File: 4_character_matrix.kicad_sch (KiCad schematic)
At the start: 24 parts, among them U22 SN74LVC244A, U23 SM411006N/15, U24 SM411006N/15, U25 SN74LVC244A, U26 SM411006N/15, U27 SM411006N/15

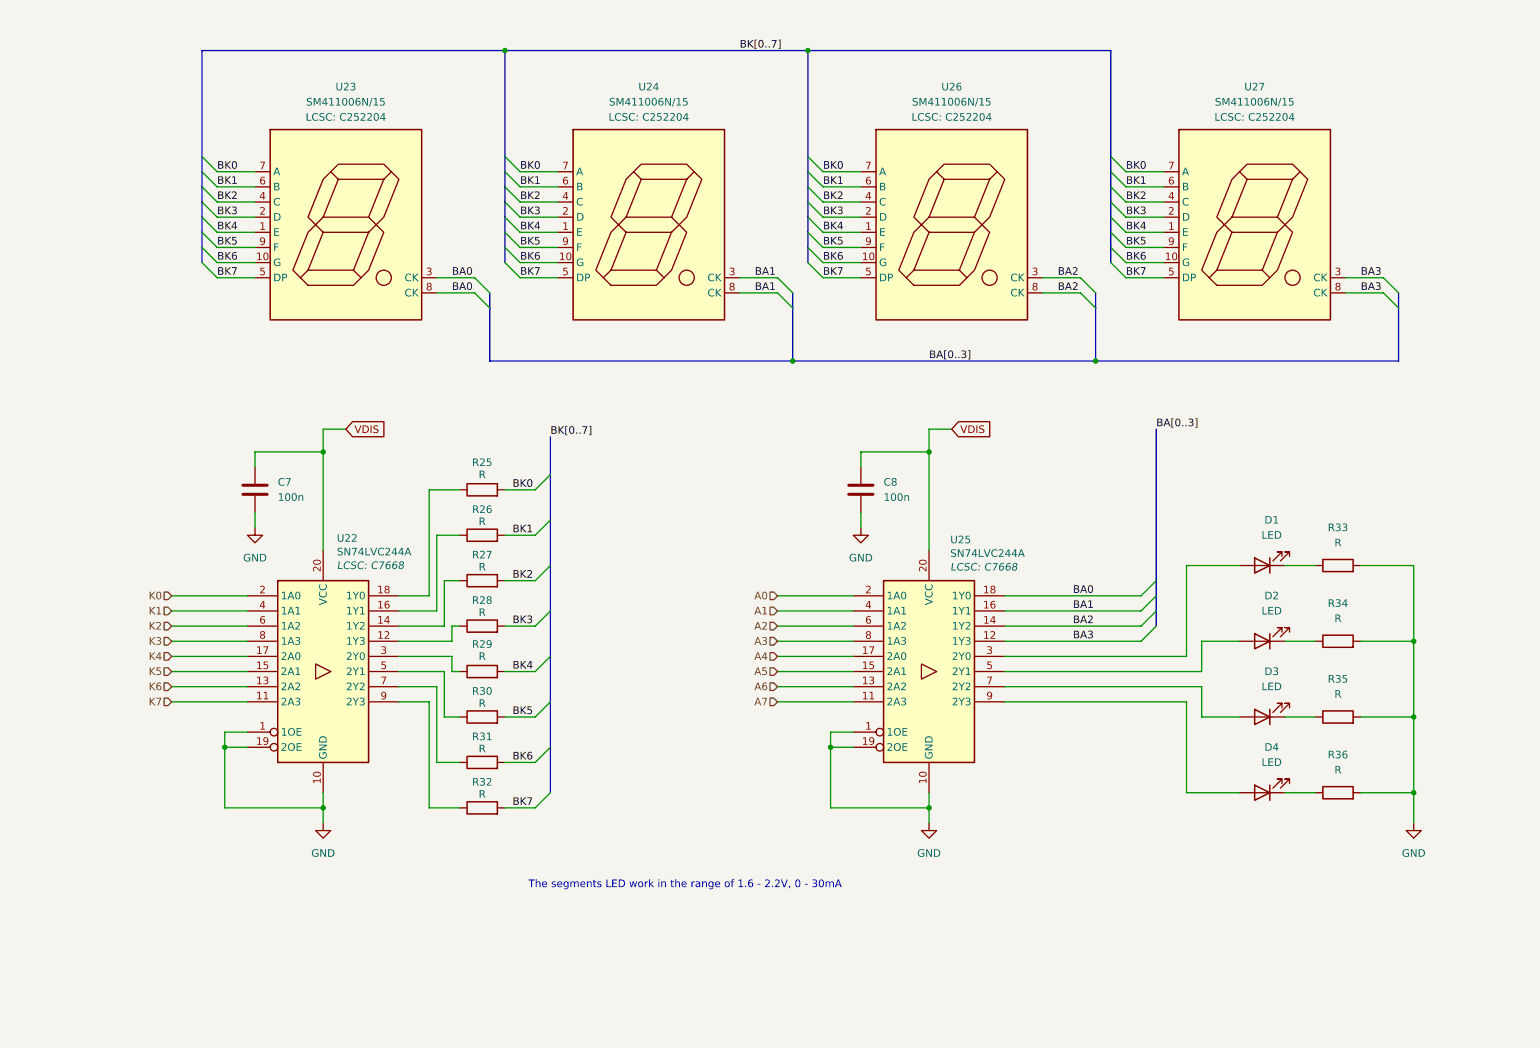
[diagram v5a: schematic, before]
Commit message: current limit resistors
- styling changes in the schematics
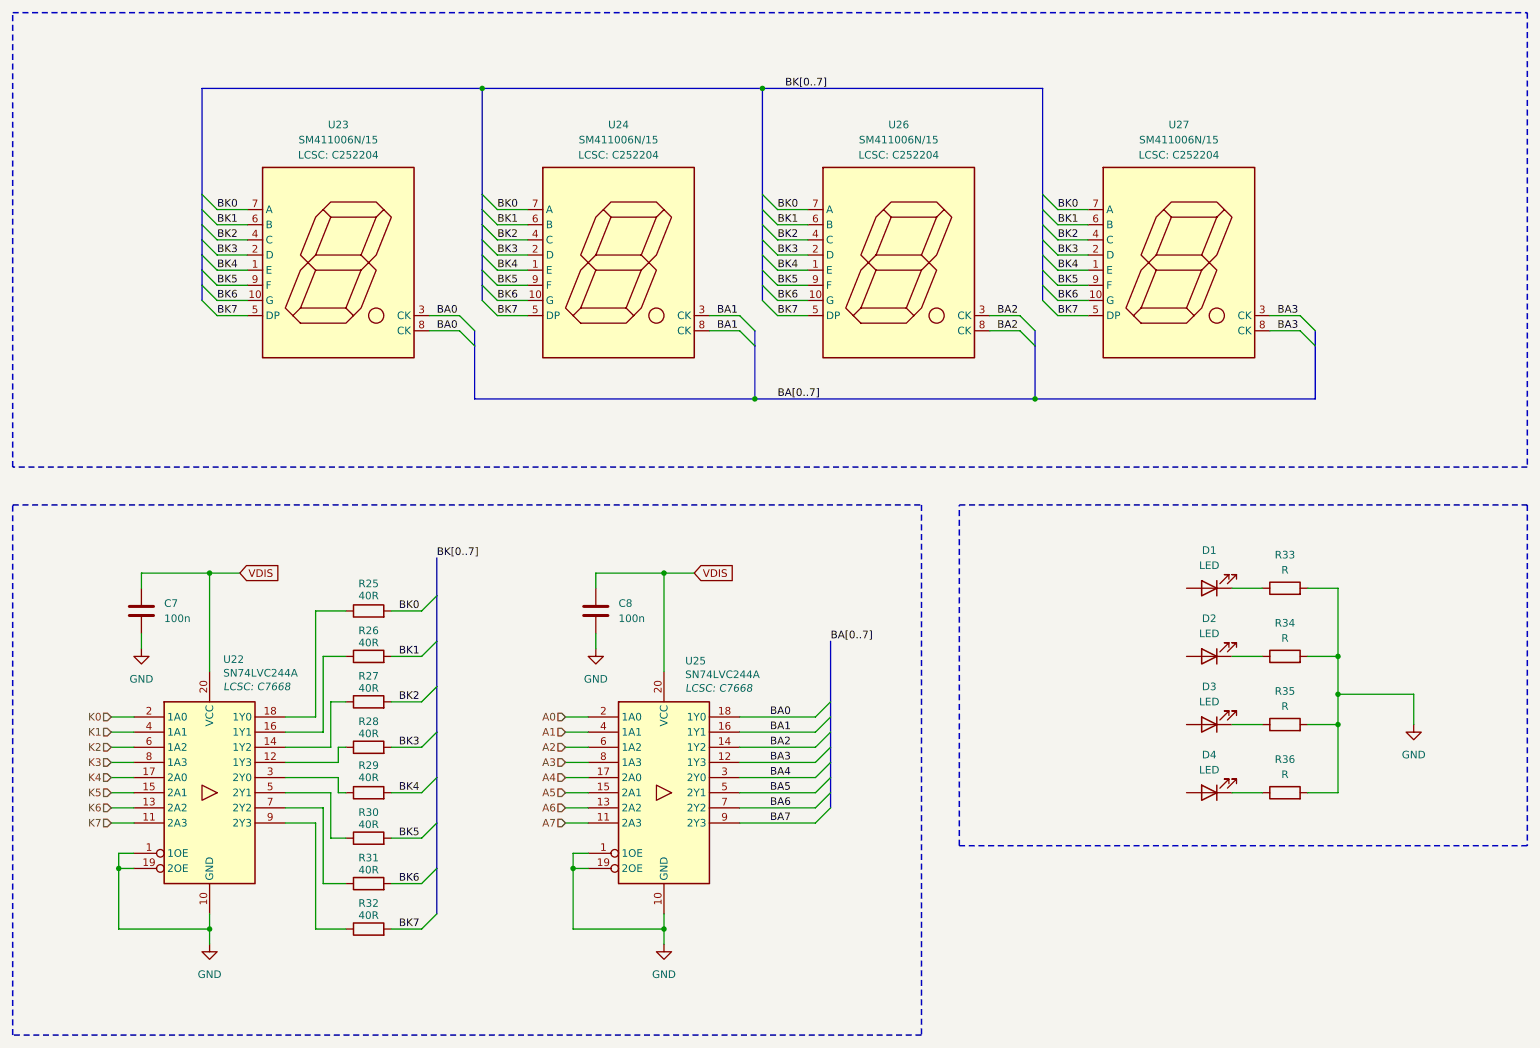
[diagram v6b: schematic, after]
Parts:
- R25, R26, R27, R28, R29, R30, R31, R32: value R -> 40R
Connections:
- net at D2.2 (A): no longer U25.5 (2Y1)
- net at D1.2 (A): no longer U25.3 (2Y0)
- net at D3.2 (A): no longer U25.7 (2Y2)
- net at D4.2 (A): no longer U25.9 (2Y3)
- new net BA4: U25.3 (2Y0)
- new net BA5: U25.5 (2Y1)
- new net BA6: U25.7 (2Y2)
- new net BA7: U25.9 (2Y3)
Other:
- note removed: "The segments LED work in the range of 1.6 - 2.2V, 0 - 30mA"
- moved on the sheet: C7, C8, D1, D2, D3, D4, R25, R26, R27, R28, R29, R30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

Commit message: minor changes
- removal of colon LEDs
- removal of test points addition of solders bridges
- time pulse LED added
- modification in MCU pinout
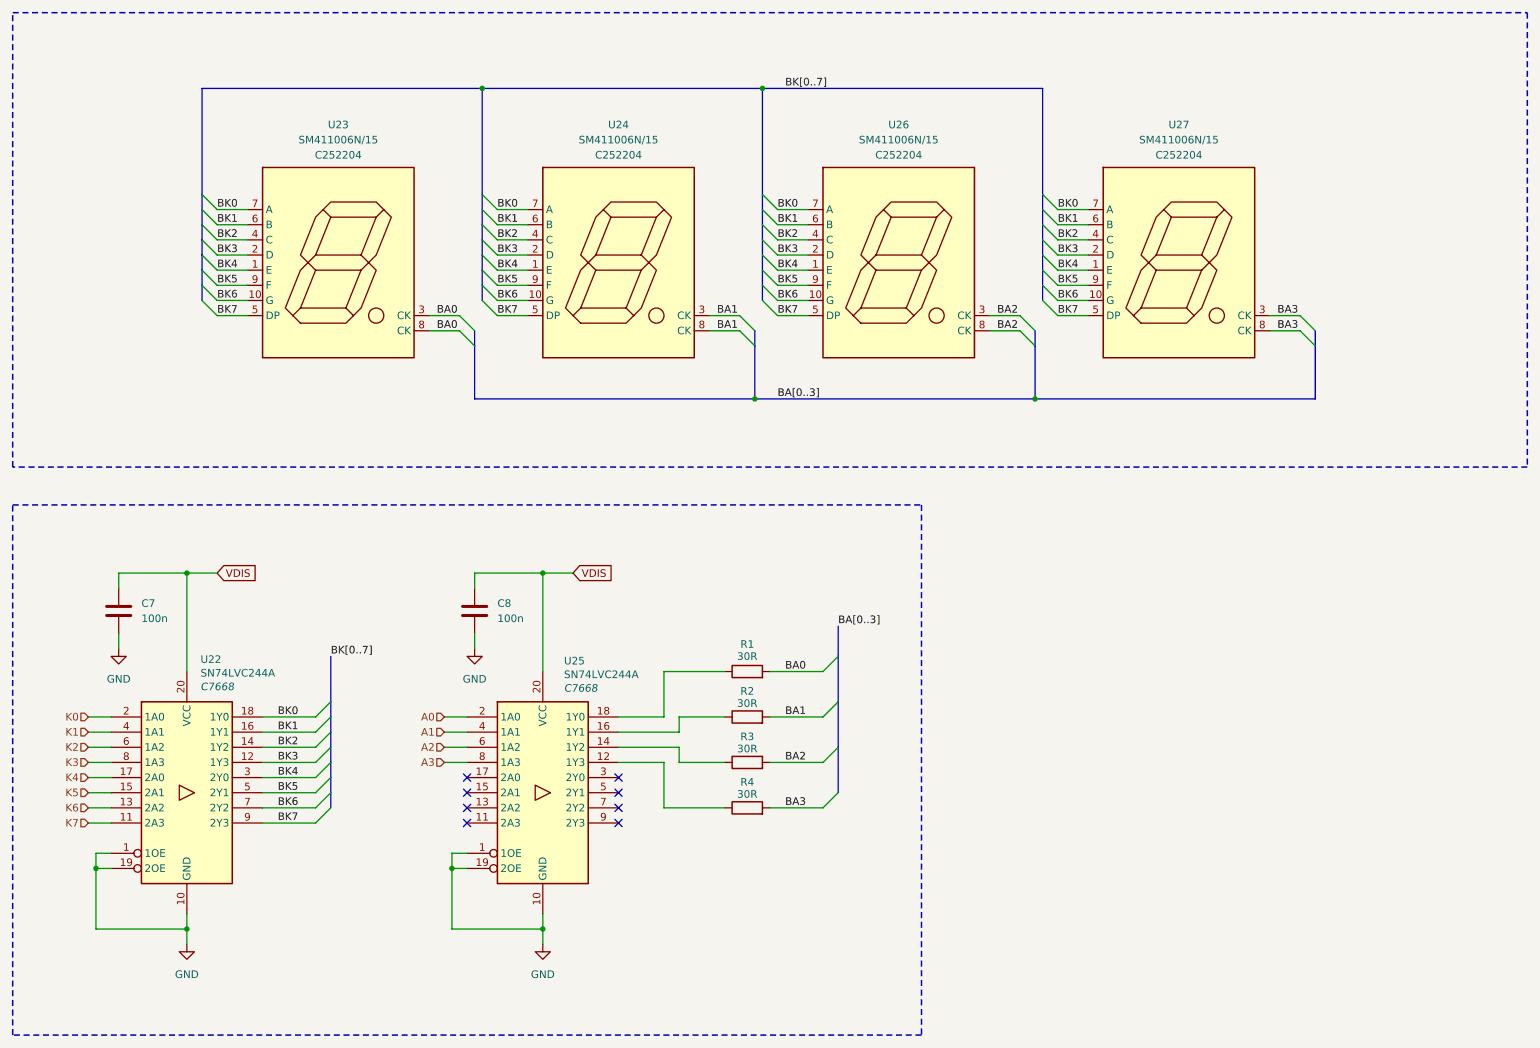
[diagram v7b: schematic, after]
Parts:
- removed D1, D2, D3, D4: LED, symbol Device:LED
- removed R25, R26, R27, R28, R29, R30, R31, R32: 40R, symbol Device:R
- removed R33, R34, R35, R36: R, symbol Device:R
- added R1, R2, R3, R4: 30R, symbol Device:R
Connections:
- net BA0: now also R1.2; no longer U25.18 (1Y0)
- net BA1: now also R2.2; no longer U25.16 (1Y1)
- net BA2: now also R3.2; no longer U25.14 (1Y2)
- net BA3: now also R4.2; no longer U25.12 (1Y3)
- net BK0: now also U22.18 (1Y0)
- net BK1: now also U22.16 (1Y1)
- net BK2: now also U22.14 (1Y2)
- net BK3: now also U22.12 (1Y3)
- net BK4: now also U22.3 (2Y0)
- net BK5: now also U22.5 (2Y1)
- net BK6: now also U22.7 (2Y2)
- net BK7: now also U22.9 (2Y3)
- net A4: no longer names the net of U25.17 (2A0)
- net A5: no longer names the net of U25.15 (2A1)
- net A6: no longer names the net of U25.13 (2A2)
- net A7: no longer names the net of U25.11 (2A3)
- net BA4: no longer names the net of U25.3 (2Y0)
- net BA5: no longer names the net of U25.5 (2Y1)
- net BA6: no longer names the net of U25.7 (2Y2)
- net BA7: no longer names the net of U25.9 (2Y3)
- new net: R4.1, U25.12 (1Y3)
- new net: R3.1, U25.14 (1Y2)
- new net: R2.1, U25.16 (1Y1)
- new net: R1.1, U25.18 (1Y0)
- no-connect marks 0 -> 8
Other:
- moved on the sheet: C7, C8, U22, U25

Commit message: minor changes
- annotations added
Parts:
- renumbered R1 to R16, R2 to R17, R3 to R18, R4 to R19, U25 to U24, U24 to U25
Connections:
- net GND: now also U24.11 (2A3), U24.13 (2A2), U24.15 (2A1), U24.17 (2A0), U24.3 (2Y0), U24.5 (2Y1), U24.7 (2Y2), U24.9 (2Y3)
- no-connect marks 8 -> 0
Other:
- note added: "4 Character matrix"
- note added: "4 Character matrix drivers"
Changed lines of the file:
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@@
 		)
 	)
+	(text "4 Character matrix drivers"
+		(exclude_from_sim no)
+		(at 21.082 186.69 0)
+		(effects
+			(font
+				(size 2.54 2.54)
+				(thickness 0.3175)
+				(color 194 0 0 1)
+			)
+			(justify left)
+		)
+	)
+	(text "4 Character matrix"
+		(exclude_from_sim no)
+		(at 21.336 91.44 0)
+		(effects
+			(font
+				(size 2.54 2.54)
+				(thickness 0.3175)
+				(color 194 0 0 1)
+			)
+			(justify left)
+		)
+	)
 	(junction
 		(at 48.26 172.72)
@@
 	)
 	(junction
+		(at 123.19 154.94)
+		(diameter 0)
+		(color 0 0 0 0)
+	)
+	(junction
 		(at 48.26 113.03)
 		(diameter 0)
@@
 	)
 	(junction
+		(at 92.71 152.4)
+		(diameter 0)
+		(color 0 0 0 0)
+	)
+	(junction
 		(at 107.95 172.72)
 		(diameter 0)
@@
 	)
 	(junction
+		(at 92.71 160.02)
+		(diameter 0)
+		(color 0 0 0 0)
+	)
+	(junction
+		(at 92.71 154.94)
+		(diameter 0)
+		(color 0 0 0 0)
+	)
+	(junction
+		(at 92.71 149.86)
+		(diameter 0)
+		(color 0 0 0 0)
+	)
+	(junction
 		(at 143.51 83.82)
 		(diameter 0)
@@
 	)
 	(junction
-		(at 190.5 83.82)
+		(at 123.19 149.86)
 		(diameter 0)
 		(color 0 0 0 0)
 	)
 	(junction
-		(at 144.78 31.75)
+		(at 190.5 83.82)
 		(diameter 0)
 		(color 0 0 0 0)
 	)
-	(no_connect
-		(at 95.25 149.86)
-	)
-	(no_connect
-		(at 120.65 147.32)
-	)
-	(no_connect
-		(at 95.25 154.94)
-	)
-	(no_connect
-		(at 120.65 149.86)
-	)
-	(no_connect
-		(at 95.25 147.32)
-	)
-	(no_connect
-		(at 95.25 152.4)
-	)
-	(no_connect
-		(at 120.65 154.94)
+	(junction
+		(at 123.19 152.4)
+		(diameter 0)
+		(color 0 0 0 0)
 	)
-	(no_connect
-		(at 120.65 152.4)
+	(junction
+		(at 144.78 31.75)
+		(diameter 0)
+		(color 0 0 0 0)
 	)
 	(bus_entry
@@
 	(wire
 		(pts
+			(xy 123.19 147.32) (xy 120.65 147.32)
+		)
+		(stroke
+			(width 0)
+			(type default)
+		)
+	)
+	(wire
+		(pts
 			(xy 33.02 160.02) (xy 33.02 162.56)
 		)
@@
 		)
 	)
+	(wire
+		(pts
+			(xy 92.71 154.94) (xy 95.25 154.94)
+		)
+		(stroke
+			(width 0)
+			(type default)
+		)
+	)
 	(bus
 		(pts
@@
 	(wire
 		(pts
+			(xy 92.71 152.4) (xy 95.25 152.4)
+		)
+		(stroke
+			(width 0)
+			(type default)
+		)
+	)
+	(wire
+		(pts
 			(xy 182.88 69.85) (xy 187.96 69.85)
 		)
@@
 		)
 	)
+	(wire
+		(pts
+			(xy 92.71 149.86) (xy 95.25 149.86)
+		)
+		(stroke
+			(width 0)
+			(type default)
+		)
+	)
 	(bus
 		(pts
@@
 	(wire
 		(pts
+			(xy 123.19 172.72) (xy 123.19 154.94)
+		)
+		(stroke
+			(width 0)
+			(type default)
+		)
+	)
+	(wire
+		(pts
 			(xy 88.9 72.39) (xy 93.98 72.39)
 		)
@@
 	(wire
 		(pts
+			(xy 120.65 149.86) (xy 123.19 149.86)
+		)
+		(stroke
+			(width 0)
+			(type default)
+		)
+	)
+	(wire
+		(pts
+			(xy 120.65 152.4) (xy 123.19 152.4)
+		)
+		(stroke
+			(width 0)
+			(type default)
+		)
+	)
+	(wire
+		(pts
 			(xy 53.34 64.77) (xy 58.42 64.77)
 		)
@@
 		)
 	)
+	(wire
+		(pts
+			(xy 92.71 147.32) (xy 95.25 147.32)
+		)
+		(stroke
+			(width 0)
+			(type default)
+		)
+	)
 	(bus
 		(pts
@@
 	(wire
 		(pts
+			(xy 92.71 152.4) (xy 92.71 149.86)
+		)
+		(stroke
+			(width 0)
+			(type default)
+		)
+	)
+	(wire
+		(pts
+			(xy 123.19 152.4) (xy 123.19 149.86)
+		)
+		(stroke
+			(width 0)
+			(type default)
+		)
+	)
+	(wire
+		(pts
 			(xy 194.31 64.77) (xy 199.39 64.77)
 		)
@@
 	(wire
 		(pts
+			(xy 120.65 154.94) (xy 123.19 154.94)
+		)
+		(stroke
+			(width 0)
+			(type default)
+		)
+	)
+	(wire
+		(pts
+			(xy 123.19 154.94) (xy 123.19 152.4)
+		)
+		(stroke
+			(width 0)
+			(type default)
+		)
+	)
+	(wire
+		(pts
 			(xy 100.33 69.85) (xy 105.41 69.85)
 		)
@@
 	(wire
 		(pts
+			(xy 92.71 154.94) (xy 92.71 152.4)
+		)
+		(stroke
+			(width 0)
+			(type default)
+		)
+	)
+	(wire
+		(pts
 			(xy 146.05 129.54) (xy 154.94 129.54)
 		)
@@
 		)
 	)
+	(wire
+		(pts
+			(xy 107.95 172.72) (xy 123.19 172.72)
+		)
+		(stroke
+			(width 0)
+			(type default)
+		)
+	)
 	(bus
 		(pts
@@
 	(wire
 		(pts
+			(xy 92.71 149.86) (xy 92.71 147.32)
+		)
+		(stroke
+			(width 0)
+			(type default)
+		)
+	)
+	(wire
+		(pts
 			(xy 194.31 67.31) (xy 199.39 67.31)
 		)
@@
 	(wire
 		(pts
+			(xy 123.19 149.86) (xy 123.19 147.32)
+		)
+		(stroke
+			(width 0)
+			(type default)
+		)
+	)
+	(wire
+		(pts
+			(xy 92.71 160.02) (xy 92.71 154.94)
+		)
+		(stroke
+			(width 0)
+			(type default)
+		)
+	)
+	(wire
+		(pts
 			(xy 53.34 69.85) (xy 58.42 69.85)
 		)
@@
 		(on_board yes)
 		(dnp no)
-		(property "Reference" "U25"
+		(property "Reference" "U24"
 			(at 111.506 127.762 0)
 			(effects
@@
 			(project "Precision Clock"
 				(path "/c9a8ff63-a0d1-4125-9dd1-40fb53daf536/d3af2bc2-13e8-43c1-8a6d-735ddffde2e2"
-					(reference "U25")
+					(reference "U24")
 					(unit 1)
 				)
@@
 		(on_board yes)
 		(dnp no)
-		(property "Reference" "R3"
+		(property "Reference" "R18"
 			(at 142.24 140.462 90)
 			(effects
@@
 			(project "Precision Clock"
 				(path "/c9a8ff63-a0d1-4125-9dd1-40fb53daf536/d3af2bc2-13e8-43c1-8a6d-735ddffde2e2"
-					(reference "R3")
+					(reference "R18")
 					(unit 1)
 				)
@@
 		(on_board yes)
 		(dnp no)
-		(property "Reference" "R1"
+		(property "Reference" "R16"
 			(at 142.24 124.968 90)
 			(effects
@@
 			(project "Precision Clock"
 				(path "/c9a8ff63-a0d1-4125-9dd1-40fb53daf536/d3af2bc2-13e8-43c1-8a6d-735ddffde2e2"
-					(reference "R1")
+					(reference "R16")
 					(unit 1)
 				)
@@
 		(on_board yes)
 		(dnp no)
-		(property "Reference" "U24"
+		(property "Reference" "U25"
 			(at 120.65 37.846 0)
 			(effects
@@
 			(project "Precision Clock"
 				(path "/c9a8ff63-a0d1-4125-9dd1-40fb53daf536/d3af2bc2-13e8-43c1-8a6d-735ddffde2e2"
-					(reference "U24")
+					(reference "U25")
 					(unit 1)
 				)
@@
 		(on_board yes)
 		(dnp no)
-		(property "Reference" "R2"
+		(property "Reference" "R17"
 			(at 142.24 132.842 90)
 			(effects
@@
 			(project "Precision Clock"
 				(path "/c9a8ff63-a0d1-4125-9dd1-40fb53daf536/d3af2bc2-13e8-43c1-8a6d-735ddffde2e2"
-					(reference "R2")
+					(reference "R17")
 					(unit 1)
 				)
@@
 		(on_board yes)
 		(dnp no)
-		(property "Reference" "R4"
+		(property "Reference" "R19"
 			(at 142.24 148.082 90)
 			(effects
@@
 			(project "Precision Clock"
 				(path "/c9a8ff63-a0d1-4125-9dd1-40fb53daf536/d3af2bc2-13e8-43c1-8a6d-735ddffde2e2"
-					(reference "R4")
+					(reference "R19")
 					(unit 1)
 				)
